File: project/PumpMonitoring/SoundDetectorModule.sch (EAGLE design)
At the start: 32 parts, among them CN1 JST-PH-K*, IC1 LMV324

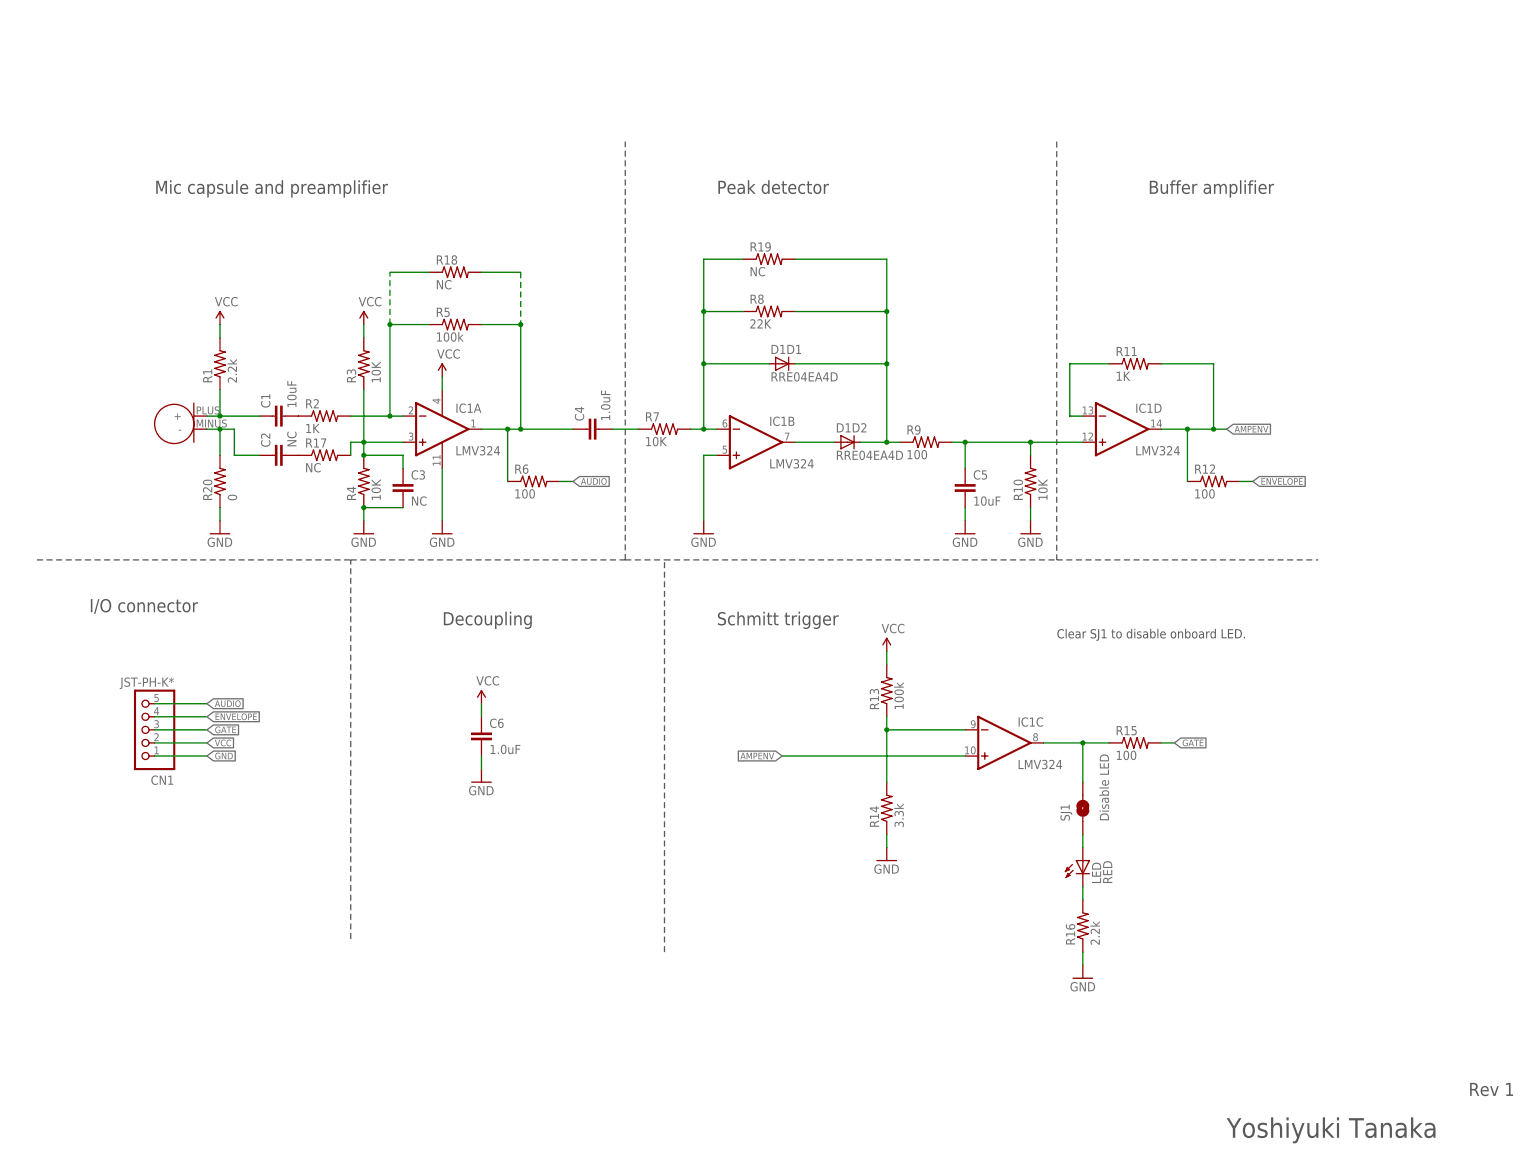
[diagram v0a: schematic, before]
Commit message: update sound detector(added license information)
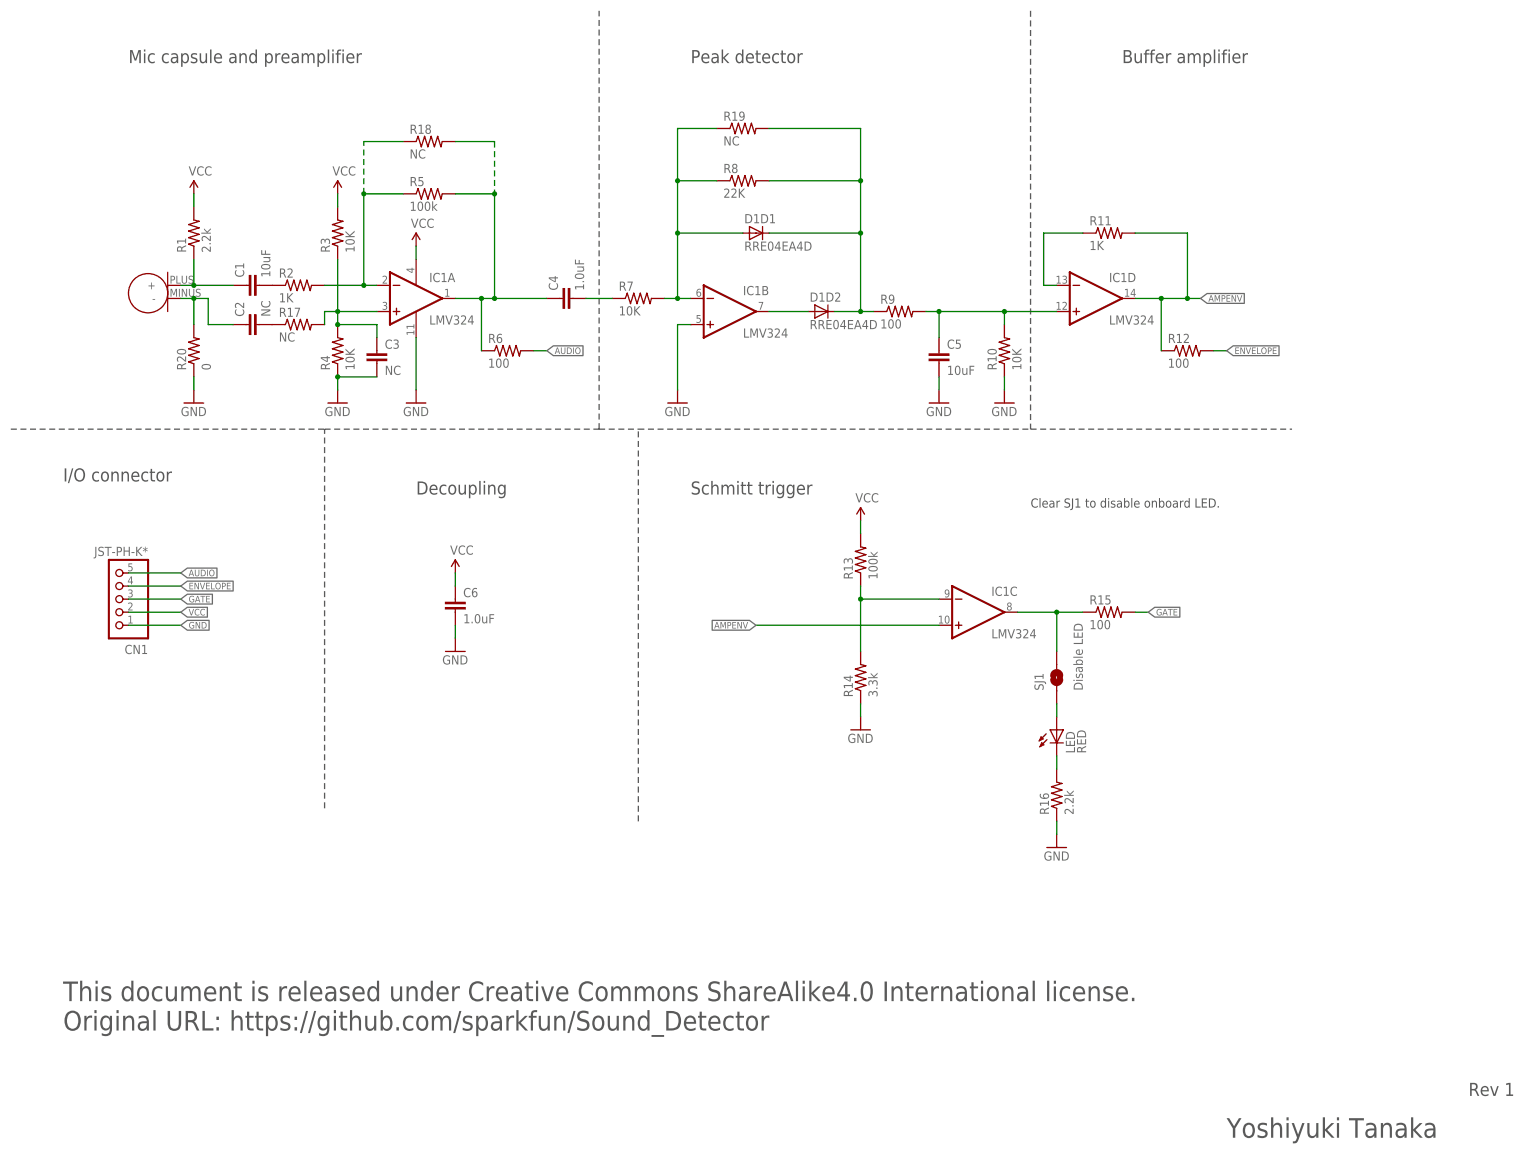
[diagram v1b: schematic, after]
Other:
- note added: "This document is released under Creative Commons ShareAlike4.0 International license. Original URL: https://github.com/sparkfun/Sound_Detector"
- moved on the sheet: C1, C2, C3, C4, C5, C6, CN1, D1D1, D1D2, IC1A, IC1B, IC1C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
